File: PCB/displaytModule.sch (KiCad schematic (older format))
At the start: 4 parts, among them M301 DisplayModule

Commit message: Corrected isolation resistor from 4.7k to 1k
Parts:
- R? (x3): value 4.7kΩ -> 1kΩ
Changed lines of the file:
@@
 LIBS:valves
 LIBS:Tfac-Symbols
+LIBS:TfaC-cache
 EELAYER 25 0
 EELAYER END
@@
 P 3050 1800
 F 0 "R?" V 3130 1800 50  0000 C CNN
-F 1 "4.7kΩ" V 3050 1800 50  0000 C CNN
+F 1 "1kΩ" V 3050 1800 50  0000 C CNN
 F 2 "" V 2980 1800 30  0000 C CNN
 F 3 "" H 3050 1800 30  0000 C CNN
@@
 P 3050 1950
 F 0 "R?" V 3130 1950 50  0000 C CNN
-F 1 "4.7kΩ" V 3050 1950 50  0000 C CNN
+F 1 "1kΩ" V 3050 1950 50  0000 C CNN
 F 2 "" V 2980 1950 30  0000 C CNN
 F 3 "" H 3050 1950 30  0000 C CNN
@@
 P 3050 2100
 F 0 "R?" V 3130 2100 50  0000 C CNN
-F 1 "4.7kΩ" V 3050 2100 50  0000 C CNN
+F 1 "1kΩ" V 3050 2100 50  0000 C CNN
 F 2 "" V 2980 2100 30  0000 C CNN
 F 3 "" H 3050 2100 30  0000 C CNN

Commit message: Trying out an alternative layout
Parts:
- removed R? (x3): 1kΩ, symbol R
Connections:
- wire segments 9 -> 6
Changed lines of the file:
@@
 Text Notes 2500 3000 0    60   ~ 0
 This will be represeted by a 5 pole angled pin header. \nThe display module will plug into this. Nothing more\nis needed here. The display module is being \ndeveloped in another project.
-$Comp
-L R R?
-U 1 1 55F1C62E
-P 3050 1800
-F 0 "R?" V 3130 1800 50  0000 C CNN
-F 1 "1kΩ" V 3050 1800 50  0000 C CNN
-F 2 "" V 2980 1800 30  0000 C CNN
-F 3 "" H 3050 1800 30  0000 C CNN
-	1    3050 1800
-	0    1    1    0
-$EndComp
-$Comp
-L R R?
-U 1 1 55F1C655
-P 3050 1950
-F 0 "R?" V 3130 1950 50  0000 C CNN
-F 1 "1kΩ" V 3050 1950 50  0000 C CNN
-F 2 "" V 2980 1950 30  0000 C CNN
-F 3 "" H 3050 1950 30  0000 C CNN
-	1    3050 1950
-	0    1    1    0
-$EndComp
-$Comp
-L R R?
-U 1 1 55F1C67F
-P 3050 2100
-F 0 "R?" V 3130 2100 50  0000 C CNN
-F 1 "1kΩ" V 3050 2100 50  0000 C CNN
-F 2 "" V 2980 2100 30  0000 C CNN
-F 3 "" H 3050 2100 30  0000 C CNN
-	1    3050 2100
-	0    1    1    0
-$EndComp
 Wire Wire Line
 	2750 1650 3300 1650
 Wire Wire Line
-	2750 1800 2900 1800
+	2750 1800 3300 1800
 Wire Wire Line
-	3200 1800 3300 1800
+	2750 1950 3300 1950
 Wire Wire Line
-	2750 1950 2900 1950
-Wire Wire Line
-	3200 1950 3300 1950
-Wire Wire Line
-	2750 2100 2900 2100
-Wire Wire Line
-	3200 2100 3300 2100
+	2750 2100 3300 2100
 $Comp
-L GND #PWR?
+L GND #PWR301
 U 1 1 55F1C70D
 P 3150 2400
-F 0 "#PWR?" H 3150 2150 50  0001 C CNN
+F 0 "#PWR301" H 3150 2150 50  0001 C CNN
 F 1 "GND" H 3150 2250 50  0000 C CNN
 F 2 "" H 3150 2400 60  0000 C CNN

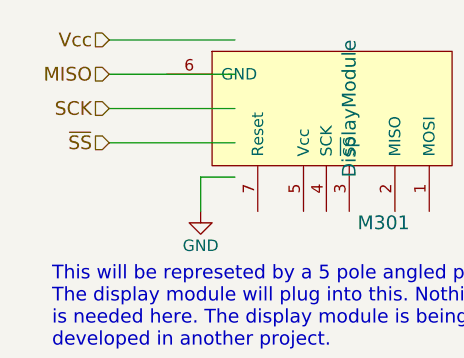
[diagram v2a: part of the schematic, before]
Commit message: Made corrections to the board for rev 2L.2
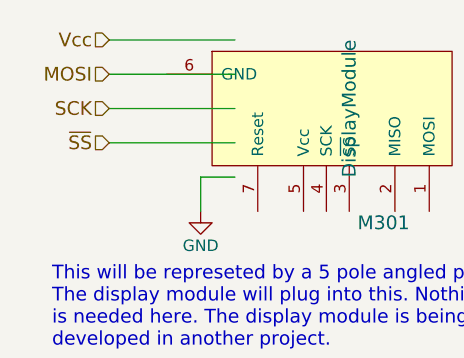
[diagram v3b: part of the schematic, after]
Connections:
- net labels added: MOSI
- net labels removed: MISO
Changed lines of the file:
@@
 Comment4 ""
 $EndDescr
-Text HLabel 2750 1800 0    60   Input ~ 0
-MISO
 Text HLabel 2750 2100 0    60   Input ~ 0
 ~SS
@@
 	2750 2100 3300 2100
 $Comp
-L GND #PWR301
+L GND #PWR06
 U 1 1 55F1C70D
 P 3150 2400
-F 0 "#PWR301" H 3150 2150 50  0001 C CNN
+F 0 "#PWR06" H 3150 2150 50  0001 C CNN
 F 1 "GND" H 3150 2250 50  0000 C CNN
 F 2 "" H 3150 2400 60  0000 C CNN
@@
 Text HLabel 2750 1950 0    60   Input ~ 0
 SCK
+Text HLabel 2750 1800 0    60   Input ~ 0
+MOSI
 $EndSCHEMATC

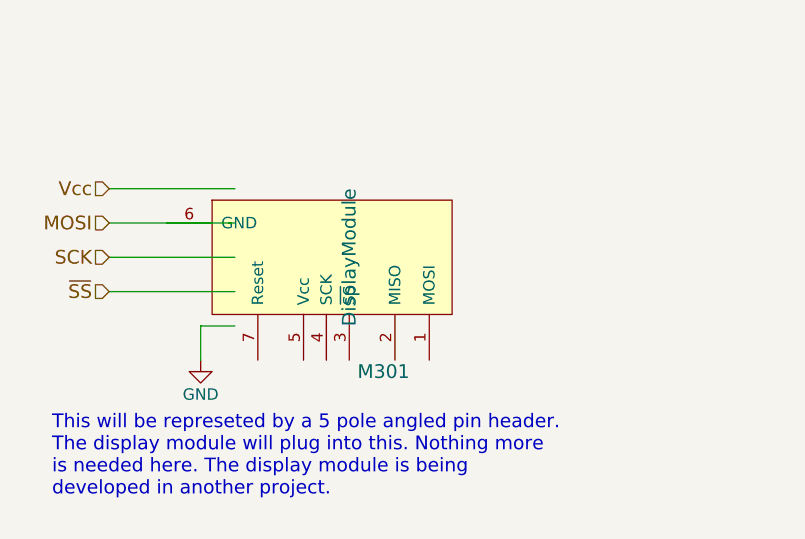
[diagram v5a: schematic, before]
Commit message: Updated the board for further features to the display
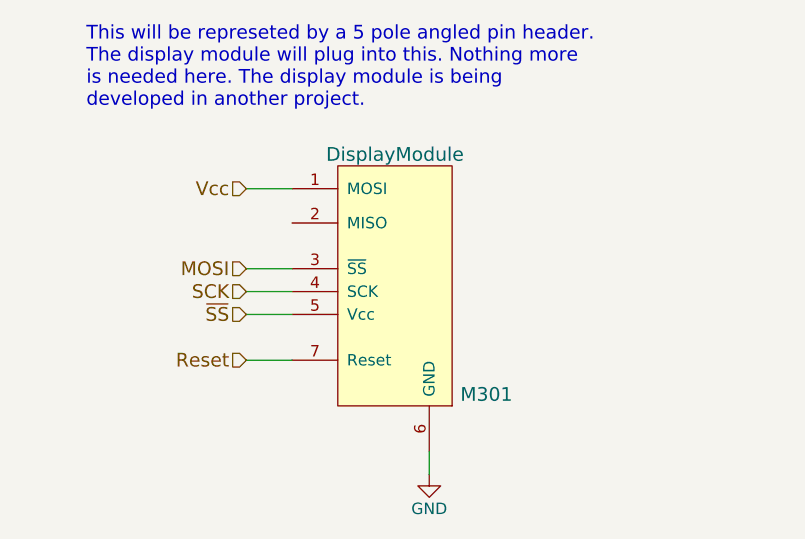
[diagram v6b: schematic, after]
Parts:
- M301: footprint Pin_Headers:Pin_Header_Straight_1x05 -> Pin_Headers:Pin_Header_Straight_1x06
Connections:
- net labels added: Reset
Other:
- moved on the sheet: M301
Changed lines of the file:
@@
 Comment4 ""
 $EndDescr
-Text HLabel 2750 2100 0    60   Input ~ 0
+Text HLabel 3350 2200 0    60   Input ~ 0
 ~SS
-Text HLabel 2750 1650 0    60   Input ~ 0
+Text HLabel 3350 1650 0    60   Input ~ 0
 Vcc
 $Comp
 L DisplayModule M301
 U 1 1 559837A8
-P 3700 1950
-F 0 "M301" V 4200 2200 60  0000 C CNN
-F 1 "DisplayModule" H 3700 2050 60  0000 C CNN
-F 2 "Pin_Headers:Pin_Header_Straight_1x05" H 3700 1950 60  0001 C CNN
-F 3 "" H 3700 1950 60  0000 C CNN
-	1    3700 1950
-	0    1    1    0
+P 4000 2100
+F 0 "M301" H 3600 1650 60  0000 C CNN
+F 1 "DisplayModule" H 4000 2700 60  0000 C CNN
+F 2 "Pin_Headers:Pin_Header_Straight_1x06" H 4000 2100 60  0001 C CNN
+F 3 "" H 4000 2100 60  0000 C CNN
+	1    4000 2100
+	-1   0    0    -1
 $EndComp
-Text Notes 2500 3000 0    60   ~ 0
+Text Notes 2650 1300 0    60   ~ 0
 This will be represeted by a 5 pole angled pin header. \nThe display module will plug into this. Nothing more\nis needed here. The display module is being \ndeveloped in another project.
 Wire Wire Line
-	2750 1650 3300 1650
+	3350 1650 3550 1650
 Wire Wire Line
-	2750 1800 3300 1800
+	3350 2000 3550 2000
 Wire Wire Line
-	2750 1950 3300 1950
-Wire Wire Line
-	2750 2100 3300 2100
+	3350 2200 3550 2200
 $Comp
 L GND #PWR08
 U 1 1 55F1C70D
-P 3150 2400
-F 0 "#PWR08" H 3150 2150 50  0001 C CNN
-F 1 "GND" H 3150 2250 50  0000 C CNN
-F 2 "" H 3150 2400 60  0000 C CNN
-F 3 "" H 3150 2400 60  0000 C CNN
-	1    3150 2400
+P 4150 2900
+F 0 "#PWR08" H 4150 2650 50  0001 C CNN
+F 1 "GND" H 4150 2750 50  0000 C CNN
+F 2 "" H 4150 2900 60  0000 C CNN
+F 3 "" H 4150 2900 60  0000 C CNN
+	1    4150 2900
 	1    0    0    -1
 $EndComp
+Text HLabel 3350 2100 0    60   Input ~ 0
+SCK
+Text HLabel 3350 2000 0    60   Input ~ 0
+MOSI
 Wire Wire Line
-	3300 2250 3150 2250
+	4150 2800 4150 2900
 Wire Wire Line
-	3150 2250 3150 2400
-Text HLabel 2750 1950 0    60   Input ~ 0
-SCK
-Text HLabel 2750 1800 0    60   Input ~ 0
-MOSI
+	3350 2100 3550 2100
+Text HLabel 3350 2400 0    60   Input ~ 0
+Reset
+Wire Wire Line
+	3350 2400 3550 2400
 $EndSCHEMATC

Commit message: Updated the routing to comply with the display module
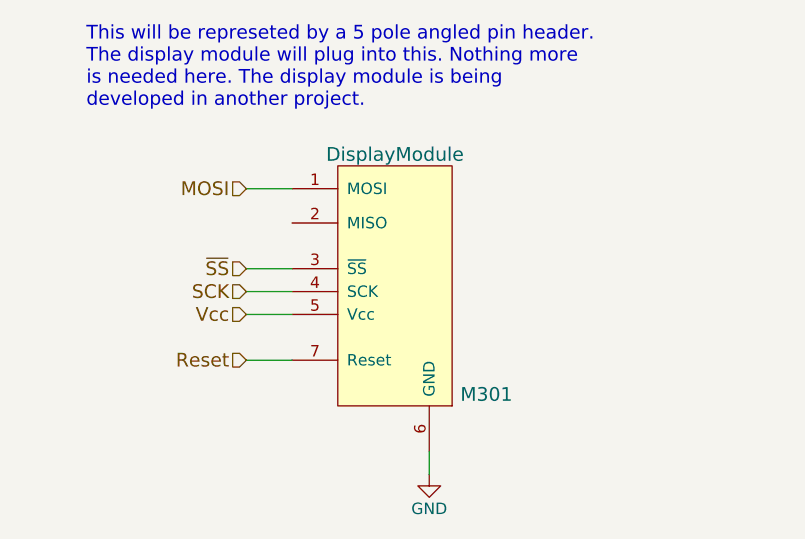
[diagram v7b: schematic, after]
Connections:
- net MOSI: now also M301.1 (MOSI); no longer M301.3 (~SS)
- net Vcc: now also M301.5 (Vcc); no longer M301.1 (MOSI)
- net ~SS: now also M301.3 (~SS); no longer M301.5 (Vcc)
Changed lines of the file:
@@
 Comment4 ""
 $EndDescr
+Text HLabel 3350 2000 0    60   Input ~ 0
+~SS
 Text HLabel 3350 2200 0    60   Input ~ 0
-~SS
-Text HLabel 3350 1650 0    60   Input ~ 0
 Vcc
 $Comp
@@
 Text HLabel 3350 2100 0    60   Input ~ 0
 SCK
-Text HLabel 3350 2000 0    60   Input ~ 0
+Text HLabel 3350 1650 0    60   Input ~ 0
 MOSI
 Wire Wire Line

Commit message: Re-organised the board to incorporate the MISO
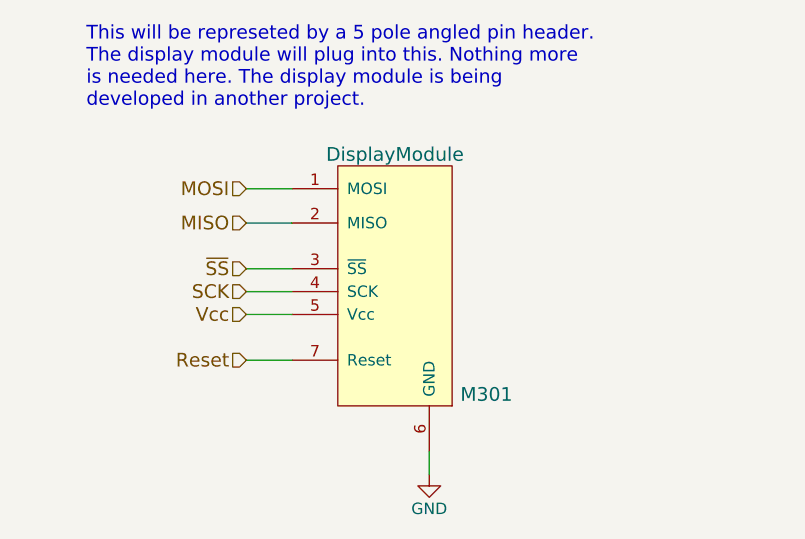
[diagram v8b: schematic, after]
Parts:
- M301: footprint Pin_Headers:Pin_Header_Straight_1x06 -> Pin_Headers:Pin_Header_Straight_1x07
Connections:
- net MISO: now reaches M301.2 (MISO)
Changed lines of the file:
@@
 F 0 "M301" H 3600 1650 60  0000 C CNN
 F 1 "DisplayModule" H 4000 2700 60  0000 C CNN
-F 2 "Pin_Headers:Pin_Header_Straight_1x06" H 4000 2100 60  0001 C CNN
+F 2 "Pin_Headers:Pin_Header_Straight_1x07" H 4000 2100 60  0001 C CNN
 F 3 "" H 4000 2100 60  0000 C CNN
 	1    4000 2100
@@
 Wire Wire Line
 	3350 2400 3550 2400
+Text HLabel 3350 1800 0    60   Input ~ 0
+MISO
+Wire Wire Line
+	3350 1800 3550 1800
 $EndSCHEMATC
